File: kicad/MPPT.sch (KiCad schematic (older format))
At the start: 0 parts

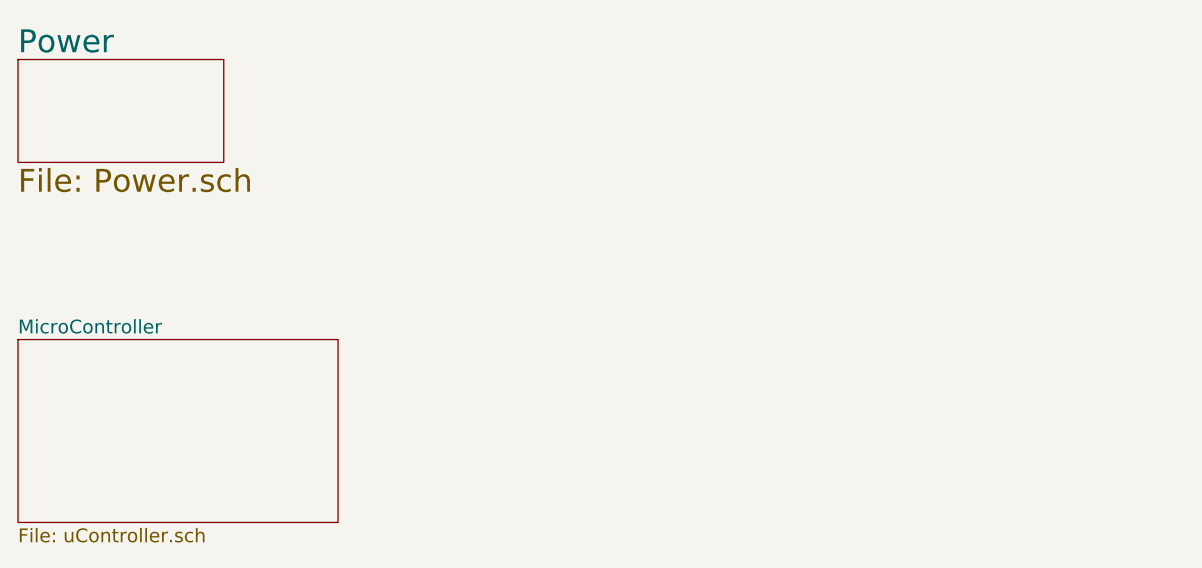
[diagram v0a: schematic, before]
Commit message: Schematical hierarchical structure enhanced
Work on schematical page KiCad
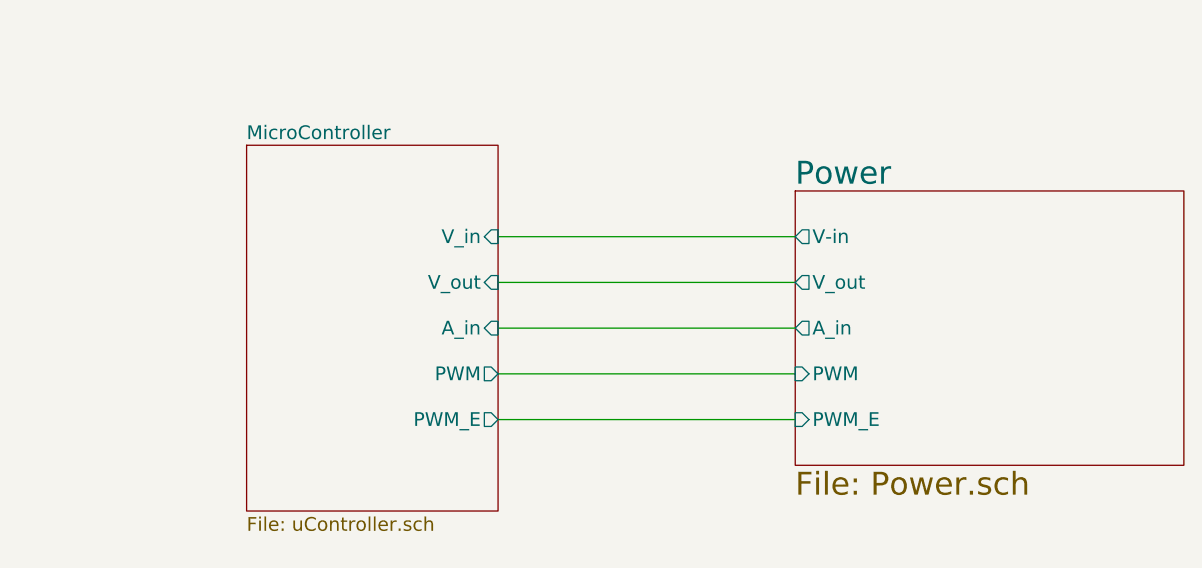
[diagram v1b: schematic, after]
